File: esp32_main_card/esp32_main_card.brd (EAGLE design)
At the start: 100 x 80 mm, 12 parts, among them J1 09231486921, J2 USB3090-XX-X_REVE, U3 ESP32-DEVKITC-32D

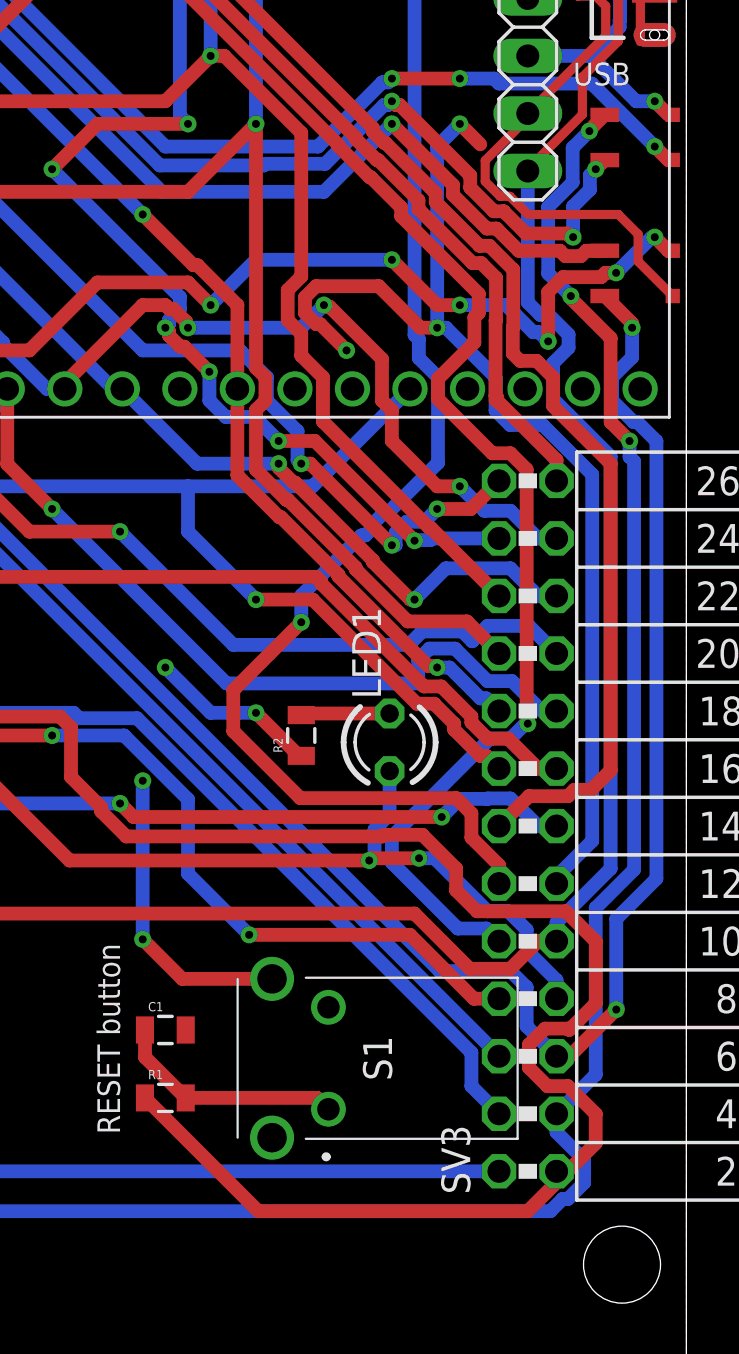
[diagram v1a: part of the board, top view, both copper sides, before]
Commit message: small mechanical changes to some cards, output connectors were moved around
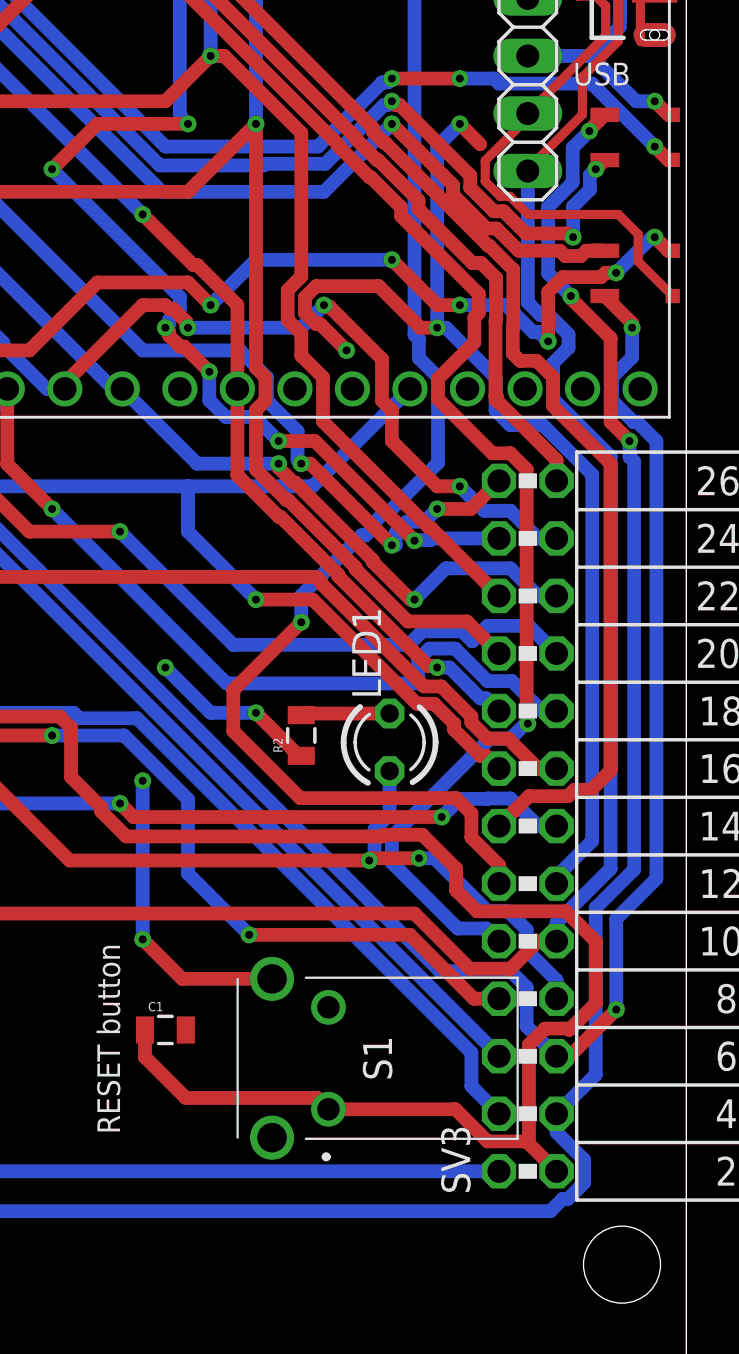
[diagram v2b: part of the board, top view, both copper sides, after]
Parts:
- removed R1: 470, SparkFun-Passives:0805
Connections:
- removed net N$8: C1.1, R1.2, S1.1
- net RESET: now also C1.1, S1.1; no longer R1.1
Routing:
- net N$8: track 10.3 -> 0.00 mm
- net RESET: track 149.6 -> 145.6 mm
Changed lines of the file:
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@@
 </layers>
 <board>
+<fusionsync huburn="a.cGVyc29uYWw6dWUyYTJjODE0" projecturn="a.cGVyc29uYWw6dWUyYWFmMDMwIzIwMjAwODE1MzIzNjg3MzAx" f3durn="urn:adsk.wipprod:dm.lineage:MBjCJ3ZTQh-woY29vzdSqA" pcbguid="" lastpulledtime="" lastsyncedchangeguid="" latestrevisionid="dd28b56f-bde6-48a5-8226-f18c79e5ae6c" lastsyncedrevisionid="dd28b56f-bde6-48a5-8226-f18c79e5ae6c" lastboardhashguid="dedc9102-e237-7193-7661-bd02f836a8b0" lastpushedtime="2021-11-11T16:50:43Z" linktopcb3d="true"/>
 <plain>
 <wire x1="0" y1="0" x2="100" y2="0" width="0" layer="20"/>
@@
 <attribute name="VALUE" x="75.984" y="14.603" size="0.4064" layer="27"/>
 </element>
-<element name="R1" library="SparkFun-Passives" package="0805" package3d_urn="urn:adsk.eagle:package:30824479/1" value="470" x="77" y="13" smashed="yes">
-<attribute name="NAME" x="76.238" y="13.8255" size="0.4064" layer="25"/>
-<attribute name="VALUE" x="75.984" y="11.603" size="0.4064" layer="27"/>
-</element>
 <element name="LED1" library="led" library_urn="urn:adsk.eagle:library:259" package="LED3MM" package3d_urn="urn:adsk.eagle:package:15797/1" value="" x="86.9" y="28.7" smashed="yes" rot="R90">
 <attribute name="COLOR" value="green" x="86.9" y="28.7" size="1.778" layer="27" rot="R90" display="off"/>
@@
 <wire x1="90.7608" y1="21.2392" x2="94.6750125" y2="21.2392" width="0.6096" layer="1"/>
 <wire x1="94.6750125" y1="21.2392" x2="96" y2="19.9142125" width="0.6096" layer="1"/>
-<wire x1="94.76" y1="9.76" x2="94.27" y2="9.76" width="0.6096" layer="1"/>
 <wire x1="88.3460375" y1="24.6162" x2="89.8354" y2="23.1268375" width="0.6096" layer="1"/>
 <wire x1="89.8354" y1="22.1646" x2="90.7608" y2="21.2392" width="0.6096" layer="1"/>
@@
 <wire x1="94.7750125" y1="16.0592" x2="93.7649875" y2="16.0592" width="0.6096" layer="1"/>
 <wire x1="93.7649875" y1="16.0592" x2="93.0508" y2="15.3450125" width="0.6096" layer="1"/>
-<wire x1="93.0508" y1="14.3349875" x2="93.0508" y2="15.3450125" width="0.6096" layer="1"/>
-<wire x1="94.7750125" y1="13.5192" x2="93.8665875" y2="13.5192" width="0.6096" layer="1"/>
-<wire x1="96" y1="11" x2="96" y2="12.2942125" width="0.6096" layer="1"/>
-<wire x1="96" y1="12.2942125" x2="94.7750125" y2="13.5192" width="0.6096" layer="1"/>
-<wire x1="93.8665875" y1="13.5192" x2="93.0508" y2="14.3349875" width="0.6096" layer="1"/>
-<contactref element="R1" pad="1"/>
-<wire x1="76.1" y1="13" x2="81.1" y2="8" width="0.6096" layer="1"/>
-<wire x1="81.1" y1="8" x2="93" y2="8" width="0.6096" layer="1"/>
-<wire x1="93" y1="8" x2="94.76" y2="9.76" width="0.6096" layer="1"/>
-<wire x1="94.76" y1="9.76" x2="96" y2="11" width="0.6096" layer="1"/>
+<contactref element="C1" pad="1"/>
+<contactref element="S1" pad="1"/>
+<wire x1="76.1" y1="14.8" x2="76.1" y2="16" width="0.6096" layer="1"/>
+<wire x1="84.2" y1="12.5" x2="89.8057875" y2="12.5" width="0.6096" layer="1"/>
+<wire x1="92.9492" y1="11.0808" x2="93.0508" y2="10.9792" width="0.6096" layer="1"/>
+<wire x1="94.015" y1="10.015" x2="94.27" y2="9.76" width="0.6096" layer="1"/>
+<wire x1="89.8057875" y1="12.5" x2="91.2249875" y2="11.0808" width="0.6096" layer="1"/>
+<wire x1="91.2249875" y1="11.0808" x2="92.9492" y2="11.0808" width="0.6096" layer="1"/>
+<wire x1="84.2" y1="12.5" x2="83.7" y2="13" width="0.6096" layer="1"/>
+<wire x1="77.9" y1="13" x2="76.1" y2="14.8" width="0.6096" layer="1"/>
+<wire x1="83.7" y1="13" x2="77.9" y2="13" width="0.6096" layer="1"/>
+<wire x1="93.0508" y1="10.9792" x2="94.015" y2="10.015" width="0.6096" layer="1"/>
+<wire x1="93.0508" y1="15.3450125" x2="93.0508" y2="10.9792" width="0.6096" layer="1"/>
 </signal>
 <signal name="USB1_D-">
@@
 <wire x1="86.1646" y1="55.6539625" x2="86.1646" y2="55.81303125" width="0.6096" layer="1"/>
 <wire x1="86.1646" y1="55.81303125" x2="75.9287375" y2="66.04889375" width="0.6096" layer="1"/>
-<wire x1="91.30436875" y1="50.618" x2="90.87025625" y2="50.618" width="0.6096" layer="1"/>
-<wire x1="90.87025625" y1="50.618" x2="88.936" y2="52.55225625" width="0.6096" layer="1"/>
-<wire x1="88.936" y1="52.55225625" x2="88.936" y2="52.94163125" width="0.6096" layer="1"/>
-<wire x1="88.936" y1="52.94163125" x2="86.71303125" y2="55.1646" width="0.6096" layer="1"/>
+<wire x1="91.30436875" y1="50.618" x2="91.25963125" y2="50.618" width="0.6096" layer="1"/>
+<wire x1="91.25963125" y1="50.618" x2="86.71303125" y2="55.1646" width="0.6096" layer="1"/>
 <wire x1="86.71303125" y1="55.1646" x2="86.6539625" y2="55.1646" width="0.6096" layer="1"/>
 <wire x1="16.0454" y1="49.6454" x2="17.8026" y2="51.4026" width="0.6096" layer="1"/>
@@
 <wire x1="52.24" y1="69.7" x2="52.24" y2="67.16" width="0.6096" layer="1"/>
 </signal>
-<signal name="N$8">
-<contactref element="C1" pad="1"/>
-<contactref element="S1" pad="1"/>
-<contactref element="R1" pad="2"/>
-<wire x1="77.9" y1="13" x2="83.7" y2="13" width="0.6096" layer="1"/>
-<wire x1="83.7" y1="13" x2="84.2" y2="12.5" width="0.6096" layer="1"/>
-<wire x1="76.1" y1="16" x2="76.1" y2="14.8" width="0.6096" layer="1"/>
-<wire x1="76.1" y1="14.8" x2="77.9" y2="13" width="0.6096" layer="1"/>
-</signal>
 <signal name="N$9">
 <contactref element="LED1" pad="K"/>
@@
 </note>
 <note version="8.3" severity="warning">
+Since Version 8.3, EAGLE supports Fusion synchronisation.
+This feature will not be available in this version and saving
+the document will break the link to the Fusion PCB feature.
+</note>
+<note version="8.3" severity="warning">

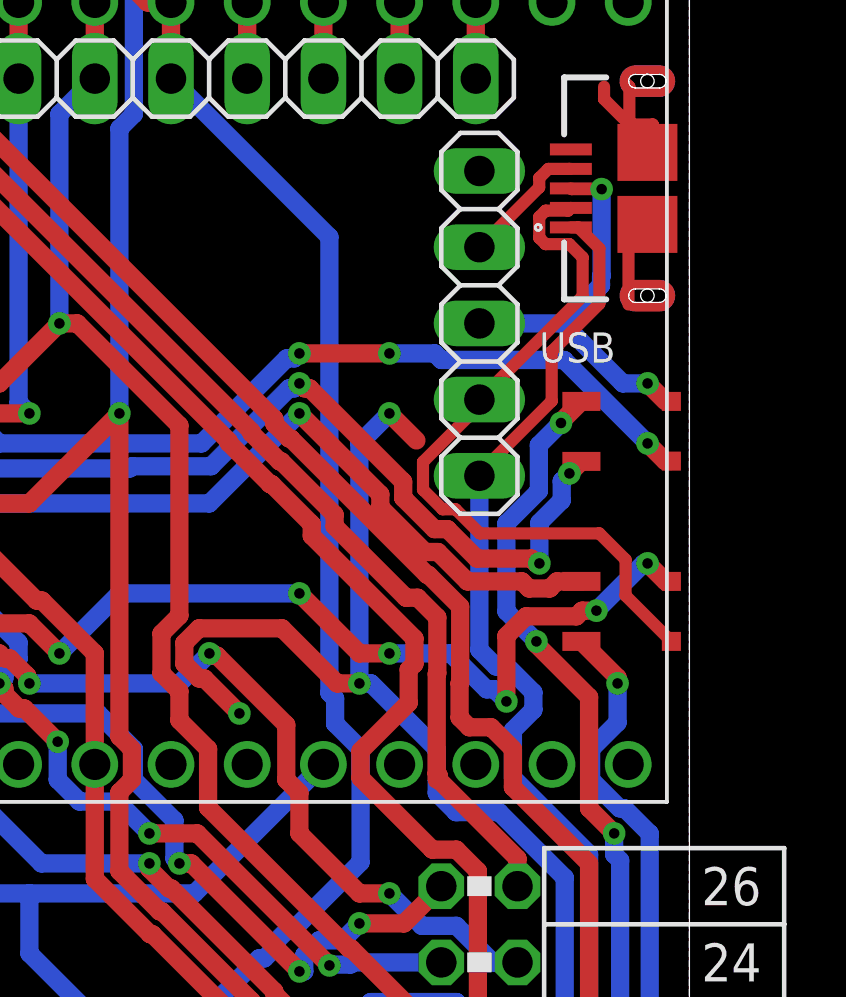
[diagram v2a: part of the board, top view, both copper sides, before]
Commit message: fixed swithc pinout on the main board
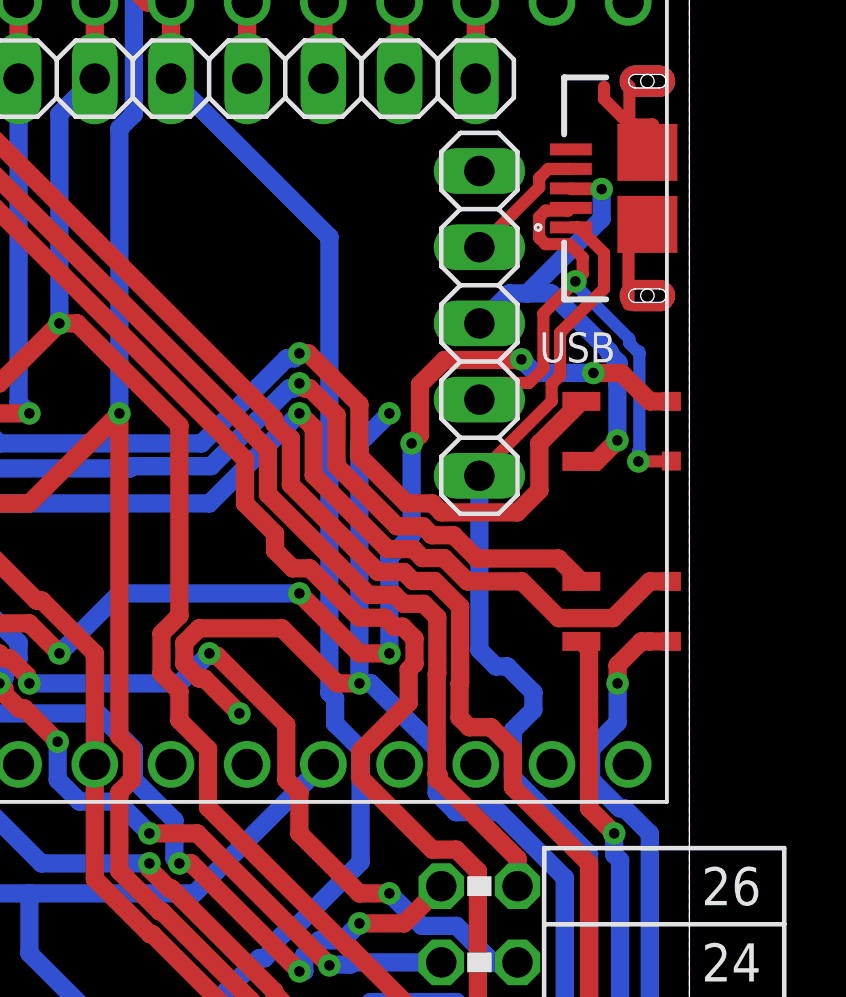
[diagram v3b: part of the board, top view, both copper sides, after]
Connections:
- net USB0_D+_IN: now also U$1.6; no longer U$1.7
- net USB0_D-_IN: now also U$1.8; no longer U$1.3
- net USB1_D+: now also U$1.1; no longer U$1.5
- net USB1_D-: now also U$1.3; no longer U$1.1
- net USB2_D+: now also U$1.2; no longer U$1.6
- net USB2_D-: now also U$1.4; no longer U$1.2
- net USB3_D+: now also U$1.5; no longer U$1.8
- net USB3_D-: now also U$1.7; no longer U$1.4
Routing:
- net USB1_D+: track 197.4 -> 187.3 mm, vias 5 -> 3
- net USB0_D-_IN: track 24.6 -> 18.5 mm, vias 0 -> 2
- net USB3_D-: track 113.6 -> 118.8 mm
- net USB2_D-: track 115.9 -> 120.4 mm
- net USB0_D+_IN: track 13.5 -> 15.7 mm
- net USB2_D+: track 112.3 -> 110.6 mm, vias 5 -> 3
- net GND: track 91.4 -> 90.2 mm
- net USB3_D+: track 105.9 -> 107.1 mm, vias 8 -> 6
- net USB1_D-: track 160.4 -> 161.5 mm
- net SCK: track 152.3 -> 153.3 mm
- net CS_2: track 148.2 -> 149.1 mm
- net CS_9: track 129.9 -> 130.6 mm
